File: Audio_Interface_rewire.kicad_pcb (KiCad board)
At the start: 2 copper layers, 62 parts, among them IC1 REG103GA-3.3_2K5, IC2 PCM2906CDB, IC3 INA849DGKT, J1 USB_B_Micro, J2 SJ-435107RS, J3 Vol. knob1 22k, J4 Vol. knob2 22k, J5 SW_PUSH_3PDT, J6 External mic. conn., Q1 J304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

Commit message: Reviewed Gnorins work
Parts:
- moved H2 2.12 mm to (97.5, 130.0)
- moved H3 1.79 mm to (189.8, 130.0)
- moved H1 1.69 mm to (97.5, 70.0)
- moved H4 0.91 mm to (189.8, 70.0)
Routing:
- net /-vs: track 14.4 -> 20.3 mm
- net /VDDI: track 16.3 -> 18.4 mm
- added copper zone on B.Cu, net GND
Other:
- board outline added: 107.5 x 75 mm
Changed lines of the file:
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@@
   )
   (footprint "MountingHole:MountingHole_4.3mm_M4_Pad" (layer "F.Cu")
-    (at 189.82 70.91)
+    (at 189.82 70)
     (descr "Mounting Hole 4.3mm, M4")
     (tags "mounting hole 4.3mm m4")
@@
   )
   (footprint "MountingHole:MountingHole_4.3mm_M4_Pad" (layer "F.Cu")
-    (at 189.812 128.21)
+    (at 189.812 130)
     (descr "Mounting Hole 4.3mm, M4")
     (tags "mounting hole 4.3mm m4")
@@
   )
   (footprint "MountingHole:MountingHole_4.3mm_M4_Pad" (layer "F.Cu")
-    (at 96.35 71.24)
+    (at 97.5 70)
     (descr "Mounting Hole 4.3mm, M4")
     (tags "mounting hole 4.3mm m4")
@@
   )
   (footprint "MountingHole:MountingHole_4.3mm_M4_Pad" (layer "F.Cu")
-    (at 96.36 128.21)
+    (at 97.5 130)
     (descr "Mounting Hole 4.3mm, M4")
     (tags "mounting hole 4.3mm m4")
@@
     )
   )
+  (gr_line (start 190 62.5) (end 97.5 62.5) (layer "Edge.Cuts") (width 0.2))
+  (gr_arc (start 97.5 137.5) (mid 92.196699 135.303301) (end 90 130) (layer "Edge.Cuts") (width 0.2))
+  (gr_line (start 190 137.5) (end 97.5 137.5) (layer "Edge.Cuts") (width 0.2))
+  (gr_arc (start 190 62.5) (mid 195.303301 64.696699) (end 197.5 70) (layer "Edge.Cuts") (width 0.2))
+  (gr_arc (start 90 70) (mid 92.196699 64.696699) (end 97.5 62.5) (layer "Edge.Cuts") (width 0.2))
+  (gr_arc (start 197.5 130) (mid 195.303301 135.303301) (end 190 137.5) (layer "Edge.Cuts") (width 0.2))
+  (gr_line (start 197.5 130) (end 197.5 70) (layer "Edge.Cuts") (width 0.2))
+  (gr_line (start 90 70) (end 90 130) (layer "Edge.Cuts") (width 0.2))
   (segment (start 134.1985 79.0215) (end 134.186 79.009) (width 0.25) (layer "F.Cu") (net 1))
   (segment (start 136.218 79.0215) (end 134.1985 79.0215) (width 0.25) (layer "F.Cu") (net 1))
@@
   (segment (start 168.19 91.29) (end 166.8 92.68) (width 0.25) (layer "F.Cu") (net 12))
   (segment (start 157.814 99.787) (end 157.814 99.137) (width 0.25) (layer "F.Cu") (net 12))
+  (segment (start 169.0045 89.2245) (end 168.934 89.154) (width 0.3) (layer "F.Cu") (net 12))
   (segment (start 166.263 95.237) (end 164.914 95.237) (width 0.25) (layer "F.Cu") (net 12))
   (segment (start 166.8 94.7) (end 166.263 95.237) (width 0.25) (layer "F.Cu") (net 12))
   (segment (start 166.8 92.68) (end 166.8 94.7) (width 0.25) (layer "F.Cu") (net 12))
   (segment (start 169.0045 91.29) (end 168.19 91.29) (width 0.25) (layer "F.Cu") (net 12))
+  (segment (start 169.0045 91.29) (end 169.0045 89.2245) (width 0.3) (layer "F.Cu") (net 12))
   (segment (start 166.63 107.297349) (end 166.63 102.7) (width 0.25) (layer "F.Cu") (net 13))
   (segment (start 166.63 102.7) (end 166.317 102.387) (width 0.25) (layer "F.Cu") (net 13))
@@
   (segment (start 132.465349 102.818651) (end 132.494 102.79) (width 0.25) (layer "F.Cu") (net 20))
   (segment (start 126.566 102.818651) (end 132.465349 102.818651) (width 0.25) (layer "F.Cu") (net 20))
+  (segment (start 131.916 114.814) (end 131.916 112.782) (width 0.3) (layer "F.Cu") (net 21))
   (segment (start 131.88 115.68) (end 131.88 114.85) (width 0.25) (layer "F.Cu") (net 21))
+  (segment (start 133.916 110.334) (end 133.916 109.734) (width 0.3) (layer "F.Cu") (net 21))
   (segment (start 136.556041 121.7) (end 136.556041 120.356041) (width 0.25) (layer "F.Cu") (net 21))
+  (segment (start 131.916 112.782) (end 132.25 112.448) (width 0.3) (layer "F.Cu") (net 21))
   (segment (start 136.894 106.137) (end 136.894 108.042) (width 0.25) (layer "F.Cu") (net 21))
+  (segment (start 132.25 112) (end 133.916 110.334) (width 0.3) (layer "F.Cu") (net 21))
   (segment (start 136.556041 120.356041) (end 131.88 115.68) (width 0.25) (layer "F.Cu") (net 21))
   (segment (start 131.88 114.85) (end 131.916 114.814) (width 0.25) (layer "F.Cu") (net 21))
+  (segment (start 132.25 112.448) (end 132.25 112) (width 0.3) (layer "F.Cu") (net 21))
   (segment (start 136.894 108.042) (end 135.202 109.734) (width 0.25) (layer "F.Cu") (net 21))
   (segment (start 135.202 109.734) (end 133.916 109.734) (width 0.25) (layer "F.Cu") (net 21))
@@
   (via (at 107.13 122.2) (size 0.8) (drill 0.4) (layers "F.Cu" "B.Cu") (net 62))
   (segment (start 107.13 122.2) (end 110.63 122.2) (width 0.25) (layer "B.Cu") (net 62))
+  (zone (net 2) (net_name "GND") (layer "B.Cu") (hatch edge 0.508)
+    (connect_pads (clearance 0.508))
+    (min_thickness 0.254) (filled_areas_thickness no)
+    (fill yes (thermal_gap 0.508) (thermal_bridge_width 0.508))
+    (polygon
+      (pts
+        (xy 200 140)
+        (xy 87.5 140)
+        (xy 87.5 60)
+        (xy 200 60)
+      )
+    )
+  )
 )

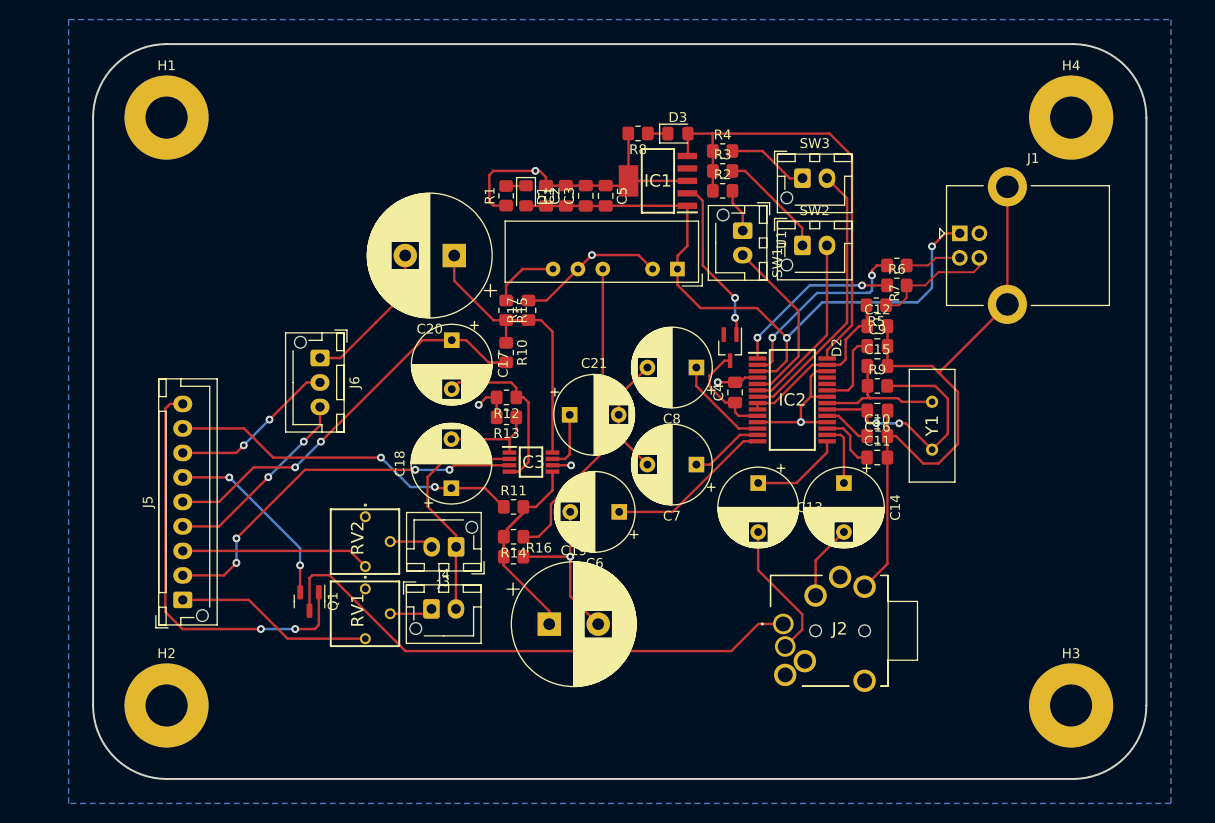
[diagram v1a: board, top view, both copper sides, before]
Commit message: Finished pcb layout for version 2.0
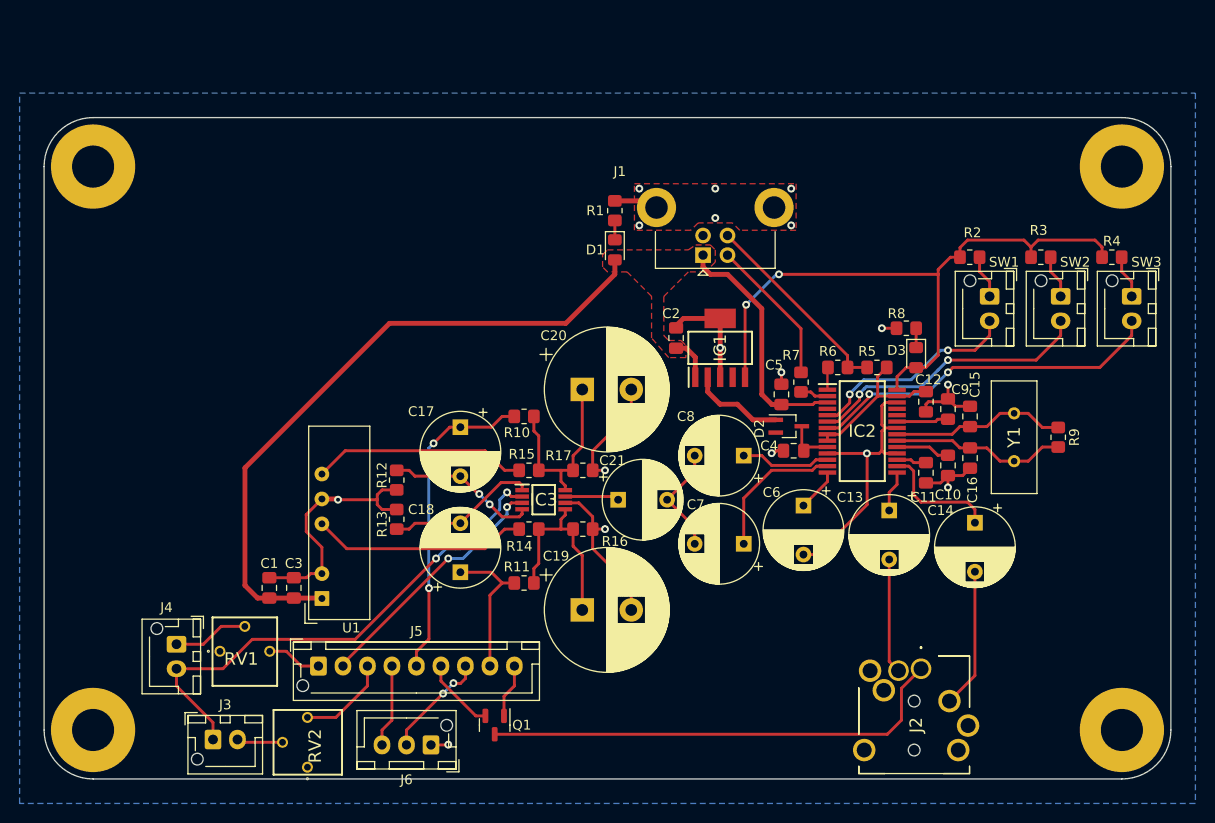
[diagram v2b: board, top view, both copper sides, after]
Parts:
- moved H1 115.8 mm to (195.0, 132.5)
- moved H2 111.9 mm to (195.0, 75.0)
- moved H4 99.9 mm to (90.0, 75.0)
- moved H3 99.8 mm to (90.0, 132.5)
- moved C1 50.2 mm to (108.0, 118.0)
- moved C3 49.9 mm to (110.5, 118.0)
- moved U1 49.5 mm to (113.4, 119.1), turned to 180 degrees
- moved R4 41.2 mm to (194.0, 84.2)
- moved J6 41.1 mm to (124.5, 134.0), turned to 180 degrees
- moved SW3 35.7 mm to (196.0, 88.2), turned to -90 degrees
- moved R8 33.8 mm to (173.0, 91.5)
- moved R3 33.6 mm to (186.7, 84.2)
- moved D3 33.4 mm to (174.0, 94.5), turned to -90 degrees
- moved J3 31.7 mm to (102.2, 133.5), turned to 0 degrees
- moved C5 27.1 mm to (160.2, 98.2)
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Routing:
- net GND: track 172.3 -> 117.3 mm, vias 7 -> 17
- net /INT_MIC_D: track 42.6 -> 5.53 mm, vias 2 -> 0
- net /RG_1: track 23.8 -> 52.3 mm, vias 0 -> 2
- net VBUS: track 68.7 -> 97.1 mm, vias 2 -> 0
- net /V_IN_D: track 36.1 -> 14.9 mm, vias 2 -> 0
- net /~{SSPND}: track 47.6 -> 65.0 mm, vias 0 -> 2
- net Net-(IC2-Pad2): track 20.0 -> 2.88 mm, vias 2 -> 0
- net Net-(IC2-Pad1): track 17.6 -> 2.30 mm, vias 2 -> 0
- net +15V: track 7.02 -> 21.9 mm
- net /hp_mic: track 20.3 -> 5.60 mm
- net /RG_2: track 39.5 -> 25.8 mm, vias 4 -> 2
- net Net-(C6-Pad1): track 17.1 -> 4.39 mm
- net /INT_MIC_S: track 19.5 -> 7.54 mm, vias 2 -> 0
- net /EXT_MIC_S: track 20.2 -> 8.47 mm, vias 2 -> 0
- net /HID1: track 18.6 -> 29.3 mm, vias 0 -> 2
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- added copper zone on F.Cu, net GND
- added copper zone on F.Cu, net VBUS
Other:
- board size 107.5 x 75 mm -> 115 x 67.5 mm

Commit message: Moved crystal closer to IC2
Moved the crystal closer to the IC2 and rewired some capacitors and resistors.
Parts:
- moved R9 9.25 mm to (179.2, 102.7)
- moved Y1 8.30 mm to (175.7, 105.1)
- moved C10 4.29 mm to (181.5, 106.1)
- moved C11 4.29 mm to (179.2, 106.8)
- moved C16 4.29 mm to (183.8, 105.3)
- moved C12 4.28 mm to (179.2, 98.5)
- moved C15 4.28 mm to (183.8, 100.0)
- moved C9 4.28 mm to (181.5, 99.2)
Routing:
- net GND: track 117.3 -> 124.1 mm, vias 17 -> 16
- net Net-(C10-Pad1): track 5.55 -> 11.5 mm
- net Net-(C11-Pad1): track 3.07 -> 8.63 mm
- net Net-(C9-Pad1): track 5.30 -> 10.8 mm
- net /VDDI: track 15.8 -> 20.3 mm
- net /XTO_Crystal: track 17.9 -> 13.7 mm
- net /XTI_Crystal: track 17.9 -> 13.8 mm

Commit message: Changed some labels
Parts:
- Audio Jack: renamed from J2
- USB MICRO: renamed from J1
- renumbered J3 to EM-KNOB, J4 to IM-KNOB, SW1 to MUTE, SW3 to V-DOWN, SW2 to V-UP
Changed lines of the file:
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@@
     (fp_line (start 5.661 1.04) (end 5.661 2.604) (layer "F.SilkS") (width 0.12))
     (fp_line (start 2.5 -4.08) (end 2.5 4.08) (layer "F.SilkS") (width 0.12))
-    (fp_line (start -1.909698 -2.315) (end -1.109698 -2.315) (layer "F.SilkS") (width 0.12))
+    (fp_line (start -2.67 -1.33) (end -1.87 -1.33) (layer "F.SilkS") (width 0.12))
     (fp_line (start 4.181 1.04) (end 4.181 3.722) (layer "F.SilkS") (width 0.12))
     (fp_line (start 4.341 1.04) (end 4.341 3.647) (layer "F.SilkS") (width 0.12))
@@
     (fp_line (start 4.021 1.04) (end 4.021 3.79) (layer "F.SilkS") (width 0.12))
     (fp_line (start 5.701 1.04) (end 5.701 2.556) (layer "F.SilkS") (width 0.12))
-    (fp_line (start -1.509698 -2.715) (end -1.509698 -1.915) (layer "F.SilkS") (width 0.12))
+    (fp_line (start -2.27 -1.73) (end -2.27 -0.93) (layer "F.SilkS") (width 0.12))
     (fp_line (start 3.741 -3.889) (end 3.741 3.889) (layer "F.SilkS") (width 0.12))
     (fp_line (start 3.901 -3.835) (end 3.901 3.835) (layer "F.SilkS") (width 0.12))
@@
     (property "Sheetname" "")
     (attr through_hole)
-    (fp_text reference "J2" (at -5.75 -0.5 90) (layer "F.SilkS")
+    (fp_text reference "Audio Jack" (at -9.35 10.7 180) (layer "F.SilkS")
       (effects (font (size 1.27 1.27) (thickness 0.254)))
     )
@@
     (property "Sheetname" "")
     (attr through_hole)
-    (fp_text reference "SW1" (at -3.5 -1.475 180) (layer "F.SilkS")
+    (fp_text reference "MUTE" (at 5.76 -0.85 180) (layer "F.SilkS")
       (effects (font (size 1 1) (thickness 0.15)))
     )
@@
     (property "Sheetname" "")
     (attr through_hole)
-    (fp_text reference "RV2" (at -0.36821 -2.74963 90) (layer "F.SilkS")
+    (fp_text reference "RV2" (at -0.0395 -3.096745 180) (layer "F.SilkS")
       (effects (font (size 1.27 1.27) (thickness 0.254)))
     )
@@
     (fp_line (start 3.3 0) (end 3.3 -6.99) (layer "F.SilkS") (width 0.2))
     (fp_line (start -3.3 -6.99) (end -3.3 0) (layer "F.SilkS") (width 0.2))
-    (fp_circle (center -3.722 -3.532) (end -3.722 -3.475) (layer "F.SilkS") (width 0.2) (fill none))
     (fp_line (start 3.3 0) (end -3.3 0) (layer "F.Fab") (width 0.2))
     (fp_line (start -3.3 -6.99) (end 3.3 -6.99) (layer "F.Fab") (width 0.2))
     (fp_line (start -3.3 0) (end -3.3 -6.99) (layer "F.Fab") (width 0.2))
     (fp_line (start 3.3 -6.99) (end 3.3 0) (layer "F.Fab") (width 0.2))
-    (pad "1" thru_hole circle locked (at -2.54 -3.53 90) (size 1.12 1.12) (drill 0.69) (layers *.Cu *.Mask)
+    (pad "1" thru_hole circle (at -2.54 -3.53 90) (size 1.12 1.12) (drill 0.69) (layers *.Cu *.Mask)
       (net 58 "unconnected-(RV2-Pad1)") (pinfunction "1") (pintype "passive"))
-    (pad "2" thru_hole circle locked (at 0 -6.07 90) (size 1.12 1.12) (drill 0.69) (layers *.Cu *.Mask)
+    (pad "2" thru_hole circle (at 0 -6.07 90) (size 1.12 1.12) (drill 0.69) (layers *.Cu *.Mask)
       (net 42 "Net-(J3-Pad2)") (pinfunction "2") (pintype "passive"))
-    (pad "3" thru_hole circle locked (at 2.54 -3.53 90) (size 1.12 1.12) (drill 0.69) (layers *.Cu *.Mask)
+    (pad "3" thru_hole circle (at 2.54 -3.53 90) (size 1.12 1.12) (drill 0.69) (layers *.Cu *.Mask)
       (net 52 "/ext_mic") (pinfunction "3") (pintype "passive"))
     (model "3362P-1-501LF.stp"
@@
     (property "Sheetname" "")
     (attr through_hole)
-    (fp_text reference "J6" (at 2.5 -3.55) (layer "F.SilkS")
+    (fp_text reference "J6" (at -3.843255 -0.285) (layer "F.SilkS")
       (effects (font (size 1 1) (thickness 0.15)))
     )
@@
     (property "Sheetname" "")
     (attr through_hole)
-    (fp_text reference "C7" (at 4.902651 4) (layer "F.SilkS")
+    (fp_text reference "C7" (at 4.992651 4.24) (layer "F.SilkS")
       (effects (font (size 1 1) (thickness 0.15)))
     )
@@
     (property "Sheetname" "")
     (attr smd)
-    (fp_text reference "IC2" (at 0 0) (layer "F.SilkS")
+    (fp_text reference "IC2" (at -0.02 0.59) (layer "F.SilkS")
       (effects (font (size 1.27 1.27) (thickness 0.254)))
     )
@@
     (property "Sheetname" "")
     (attr smd)
-    (fp_text reference "IC3" (at 0 0) (layer "F.SilkS")
+    (fp_text reference "IC3" (at 0.103255 -0.21 90) (layer "F.SilkS")
       (effects (font (size 1.27 1.27) (thickness 0.254)))
     )
@@
     (property "Sheetname" "")
     (attr through_hole)
-    (fp_text reference "SW2" (at -3.5 -1.475 180) (layer "F.SilkS")
+    (fp_text reference "V-UP" (at 6.13 -0.58 180) (layer "F.SilkS")
       (effects (font (size 1 1) (thickness 0.15)))
     )
@@
     (property "Sheetname" "")
     (attr through_hole)
-    (fp_text reference "J3" (at 1.25 -3.55) (layer "F.SilkS")
+    (fp_text reference "EM-KNOB" (at 2.563255 -3.55) (layer "F.SilkS")
       (effects (font (size 1 1) (thickness 0.15)))
     )
@@
     (property "Sheetname" "")
     (attr through_hole)
-    (fp_text reference "C21" (at -0.584094 -4) (layer "F.SilkS")
+    (fp_text reference "C21" (at -0.664094 -4.08) (layer "F.SilkS")
       (effects (font (size 1 1) (thickness 0.15)))
     )
@@
     (property "Sheetname" "")
     (attr through_hole)
-    (fp_text reference "RV1" (at -0.36821 -2.74963) (layer "F.SilkS")
+    (fp_text reference "RV1" (at 0.513255 -1.78) (layer "F.SilkS")
       (effects (font (size 1.27 1.27) (thickness 0.254)))
     )
@@
     (property "Sheetname" "")
     (attr through_hole)
-    (fp_text reference "J4" (at -3.75 1.025 180) (layer "F.SilkS")
+    (fp_text reference "IM-KNOB" (at -3.75 0.511745 180) (layer "F.SilkS")
       (effects (font (size 1 1) (thickness 0.15)))
     )
@@
     (property "Sheetname" "")
     (attr through_hole)
-    (fp_text reference "J1" (at 8.5375 -8.5 180) (layer "F.SilkS")
+    (fp_text reference "USB MICRO" (at 11.8675 12.69 180) (layer "F.SilkS")
       (effects (font (size 1 1) (thickness 0.15)))
     )
@@
     (property "Sheetname" "")
     (attr through_hole)
-    (fp_text reference "SW3" (at -3.5 -1.5) (layer "F.SilkS")
+    (fp_text reference "V-DOWN" (at 6.18 0.54) (layer "F.SilkS")
       (effects (font (size 1 1) (thickness 0.15)))
     )
@@
     (property "Sheetname" "")
     (attr smd)
-    (fp_text reference "IC1" (at 0 0 90) (layer "F.SilkS")
+    (fp_text reference "IC1" (at 0.04 1.23 90) (layer "F.SilkS")
       (effects (font (size 1.27 1.27) (thickness 0.254)))
     )
@@
     (property "Sheetname" "")
     (attr through_hole)
-    (fp_text reference "C19" (at -2.676041 -5.5 180) (layer "F.SilkS")
+    (fp_text reference "C19" (at -2.696041 -5.59 180) (layer "F.SilkS")
       (effects (font (size 1 1) (thickness 0.15)))
     )

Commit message: Fixed the final design
Added a logo and fixed some readabiliy and cosmetics for the PCB
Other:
- board text added: "Audio Interface"
- board text added: "Made by: Gadden & Fasbjorn"
